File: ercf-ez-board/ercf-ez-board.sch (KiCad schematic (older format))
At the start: 27 parts, among them J1 Conn_01x03_Male, J2 Conn_01x03_Male, J3 Conn_01x03_Male, J4 Conn_01x03_Male, J5 Screw_Terminal_01x02, J6 Conn_01x05_Male, J7 Conn_01x04_Male, J8 Conn_01x04_Male, U1 SeeeduinoXIAO, U2 L7805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

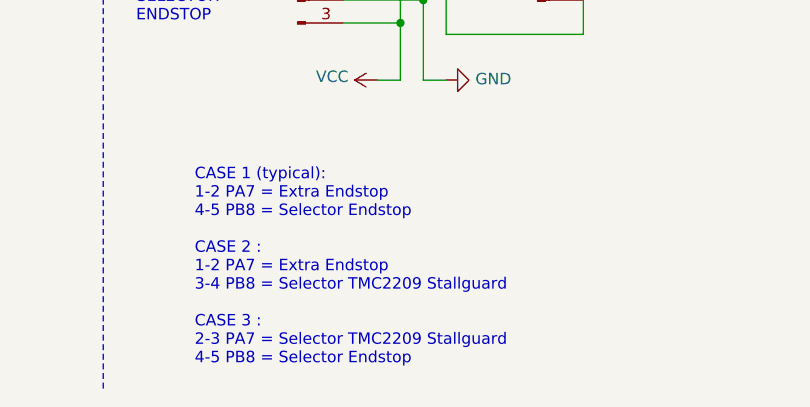
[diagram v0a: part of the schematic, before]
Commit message: Fix comment on schematic and layout
Fix comment on schematic and layout
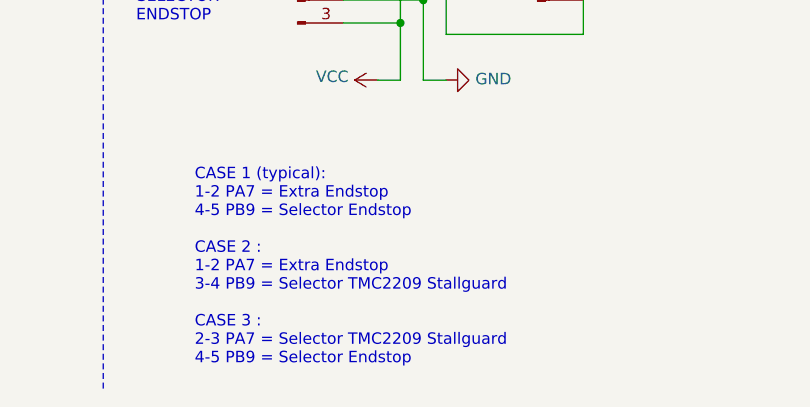
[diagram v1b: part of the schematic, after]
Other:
- note added: "CASE 1 (typical):\n1-2 PA7 = Extra Endstop\n4-5 PB9 = Selector Endstop\n\nCASE 2 : \n1-2 PA7 = Extra Endstop\n3-4 PB9 = Selector TMC2209 Stallguard\n\nCASE 3 : \n2-3 PA7 = Selector TMC2209 Stallguard\n4-5 PB9 = Selector Endstop"
- note removed: "CASE 1 (typical):\n1-2 PA7 = Extra Endstop\n4-5 PB8 = Selector Endstop\n\nCASE 2 : \n1-2 PA7 = Extra Endstop\n3-4 PB8 = Selector TMC2209 Stallguard\n\nCASE 3 : \n2-3 PA7 = Selector TMC2209 Stallguard\n4-5 PB8 = Selector Endstop"
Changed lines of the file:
@@
 Sheet 1 1
 Title "ERCF EZ BOARD"
-Date "29/05/2021"
+Date "31/05/2021"
 Rev "v1.0"
 Comp "The ERCF fanclub"
@@
 - SELECTOR \n  ENDSTOP
 Text Notes 4700 7650 0    50   ~ 0
-CASE 1 (typical):\n1-2 PA7 = Extra Endstop\n4-5 PB8 = Selector Endstop\n\nCASE 2 : \n1-2 PA7 = Extra Endstop\n3-4 PB8 = Selector TMC2209 Stallguard\n\nCASE 3 : \n2-3 PA7 = Selector TMC2209 Stallguard\n4-5 PB8 = Selector Endstop
+CASE 1 (typical):\n1-2 PA7 = Extra Endstop\n4-5 PB9 = Selector Endstop\n\nCASE 2 : \n1-2 PA7 = Extra Endstop\n3-4 PB9 = Selector TMC2209 Stallguard\n\nCASE 3 : \n2-3 PA7 = Selector TMC2209 Stallguard\n4-5 PB9 = Selector Endstop
 Text Notes 8650 5850 0    50   ~ 0
 stallguard
